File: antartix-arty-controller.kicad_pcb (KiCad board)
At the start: 2 copper layers, 50.3 x 45.6 mm, 31 parts, among them J1 QTE-020-04-L-D-A, J2 73725-0110BLF, J3 73725-0110BLF, J4 73725-0110BLF, U1 PCT2075GVX, U2 PAC1934T-I_JQ, U3 USB2514B-I_M2, U4 TPS2051BDBVR, U5 TPS2051BDBVR, U6 TPS2051BDBVR, Y1 7C-24.000MBB-T

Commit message: Add FTDI and clean up schematic
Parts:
- C1, C2, C3, C4, C5, C6, C7, C8: footprint antmicro-footprints:0402-cap -> antartix-arty-controller-footprints:0402-cap
- D1: footprint antmicro-footprints:LED_0603 -> antartix-arty-controller-footprints:LED_0603
- J1: footprint antmicro-footprints:QTE-020-04-L-D-A -> antartix-arty-controller-footprints:QTE-020-04-L-D-A
- J2, J3, J4: footprint antmicro-footprints:USB_A_Female_Vertical_RA_73725-0110BLF -> antartix-arty-controller-footprints:USB_A_Female_Vertical_RA_73725-0110BLF
- R1, R10, R11, R2, R3, R4, R5, R9: footprint antmicro-footprints:0402-res -> antartix-arty-controller-footprints:0402-res
- R6, R7, R8: footprint antmicro-footprints:1206-res -> antartix-arty-controller-footprints:1206-res
- U1: footprint antmicro-footprints:SOT95P275X110-6N -> antartix-arty-controller-footprints:SOT95P275X110-6N
- U2: footprint antmicro-footprints:QFN65P400X400X55-17N -> antartix-arty-controller-footprints:QFN65P400X400X55-17N
- U3: footprint antmicro-footprints:QFN50P600X600X100-37N -> antartix-arty-controller-footprints:QFN50P600X600X100-37N
- U4, U5, U6: footprint antmicro-footprints:SOT-753 -> antartix-arty-controller-footprints:SOT-753
- Y1: footprint antmicro-footprints:7C-24.000MBB-T -> antartix-arty-controller-footprints:7C-24.000MBB-T
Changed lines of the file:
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@@
     (add_net VCC5V0)
   )
-  (module antmicro-footprints:7C-24.000MBB-T (layer F.Cu)
+  (module antartix-arty-controller-footprints:7C-24.000MBB-T (layer F.Cu)
     (at 146.325 69.8 180)
     (attr smd)
@@
     )
   )
-  (module antmicro-footprints:SOT-753 (layer F.Cu)
+  (module antartix-arty-controller-footprints:SOT-753 (layer F.Cu)
     (at 149.85 86.35)
     (attr smd)
@@
     )
   )
-  (module antmicro-footprints:SOT-753 (layer F.Cu)
+  (module antartix-arty-controller-footprints:SOT-753 (layer F.Cu)
     (at 145.75 86.35)
     (attr smd)
@@
     )
   )
-  (module antmicro-footprints:SOT-753 (layer F.Cu)
+  (module antartix-arty-controller-footprints:SOT-753 (layer F.Cu)
     (at 141.725 86.4)
     (attr smd)
@@
     )
   )
-  (module antmicro-footprints:QFN50P600X600X100-37N (layer F.Cu)
+  (module antartix-arty-controller-footprints:QFN50P600X600X100-37N (layer F.Cu)
     (at 146.2 77.125)
     (fp_text reference U3 (at -1.537438 -4.195475) (layer F.SilkS)
@@
     )
   )
-  (module antmicro-footprints:QFN65P400X400X55-17N (layer F.Cu)
+  (module antartix-arty-controller-footprints:QFN65P400X400X55-17N (layer F.Cu)
     (at 132.55 86.55 180)
     (fp_text reference U2 (at 0.371485 -3.250455) (layer F.SilkS)
@@
     )
   )
-  (module antmicro-footprints:SOT95P275X110-6N (layer F.Cu)
+  (module antartix-arty-controller-footprints:SOT95P275X110-6N (layer F.Cu)
     (at 133.47 74.525)
     (fp_text reference U1 (at -0.508 -2.286) (layer F.SilkS)
@@
     )
   )
-  (module antmicro-footprints:0402-res (layer F.Cu)
+  (module antartix-arty-controller-footprints:0402-res (layer F.Cu)
     (at 141.45 79.35 180)
     (descr "Resistor SMD 0402 (1005 Metric), square (rectangular) end terminal, IPC_7351 nominal, (Body size source: http://www.tortai-tech.com/upload/download/2011102023233369053.pdf), generated with kicad-footprint-generator")
@@
     )
   )
-  (module antmicro-footprints:0402-res (layer F.Cu)
+  (module antartix-arty-controller-footprints:0402-res (layer F.Cu)
     (at 141.45 78.35 180)
     (descr "Resistor SMD 0402 (1005 Metric), square (rectangular) end terminal, IPC_7351 nominal, (Body size source: http://www.tortai-tech.com/upload/download/2011102023233369053.pdf), generated with kicad-footprint-generator")
@@
     )
   )
-  (module antmicro-footprints:0402-res (layer F.Cu)
+  (module antartix-arty-controller-footprints:0402-res (layer F.Cu)
     (at 145.21 72.775)
     (descr "Resistor SMD 0402 (1005 Metric), square (rectangular) end terminal, IPC_7351 nominal, (Body size source: http://www.tortai-tech.com/upload/download/2011102023233369053.pdf), generated with kicad-footprint-generator")
@@
     )
   )
-  (module antmicro-footprints:1206-res (layer F.Cu)
+  (module antartix-arty-controller-footprints:1206-res (layer F.Cu)
     (at 148.9 91.625 90)
     (descr http://media.digikey.com/pdf/Data%20Sheets/Lite-On%20PDFs/LTST-C230KFKT_5-24-06.pdf)
@@
     )
   )
-  (module antmicro-footprints:1206-res (layer F.Cu)
+  (module antartix-arty-controller-footprints:1206-res (layer F.Cu)
     (at 144.775 91.375 90)
     (descr http://media.digikey.com/pdf/Data%20Sheets/Lite-On%20PDFs/LTST-C230KFKT_5-24-06.pdf)
@@
     )
   )
-  (module antmicro-footprints:1206-res (layer F.Cu)
+  (module antartix-arty-controller-footprints:1206-res (layer F.Cu)
     (at 140.775 91.725 90)
     (descr http://media.digikey.com/pdf/Data%20Sheets/Lite-On%20PDFs/LTST-C230KFKT_5-24-06.pdf)
@@
     )
   )
-  (module antmicro-footprints:0402-res (layer F.Cu)
+  (module antartix-arty-controller-footprints:0402-res (layer F.Cu)
     (at 151.075 77.625 180)
     (descr "Resistor SMD 0402 (1005 Metric), square (rectangular) end terminal, IPC_7351 nominal, (Body size source: http://www.tortai-tech.com/upload/download/2011102023233369053.pdf), generated with kicad-footprint-generator")
@@
     )
   )
-  (module antmicro-footprints:0402-res (layer F.Cu)
+  (module antartix-arty-controller-footprints:0402-res (layer F.Cu)
     (at 151.075 76.625 180)
     (descr "Resistor SMD 0402 (1005 Metric), square (rectangular) end terminal, IPC_7351 nominal, (Body size source: http://www.tortai-tech.com/upload/download/2011102023233369053.pdf), generated with kicad-footprint-generator")
@@
     )
   )
-  (module antmicro-footprints:0402-res (layer F.Cu)
+  (module antartix-arty-controller-footprints:0402-res (layer F.Cu)
     (at 151.075 75.125)
     (descr "Resistor SMD 0402 (1005 Metric), square (rectangular) end terminal, IPC_7351 nominal, (Body size source: http://www.tortai-tech.com/upload/download/2011102023233369053.pdf), generated with kicad-footprint-generator")
@@
     )
   )
-  (module antmicro-footprints:0402-res (layer F.Cu)
+  (module antartix-arty-controller-footprints:0402-res (layer F.Cu)
     (at 151.075 74.1 180)
     (descr "Resistor SMD 0402 (1005 Metric), square (rectangular) end terminal, IPC_7351 nominal, (Body size source: http://www.tortai-tech.com/upload/download/2011102023233369053.pdf), generated with kicad-footprint-generator")
@@
     )
   )
-  (module antmicro-footprints:0402-res (layer F.Cu)
+  (module antartix-arty-controller-footprints:0402-res (layer F.Cu)
     (at 168.375 88.65 90)
     (descr "Resistor SMD 0402 (1005 Metric), square (rectangular) end terminal, IPC_7351 nominal, (Body size source: http://www.tortai-tech.com/upload/download/2011102023233369053.pdf), generated with kicad-footprint-generator")
@@
     )
   )
-  (module antmicro-footprints:USB_A_Female_Vertical_RA_73725-0110BLF (layer F.Cu)
+  (module antartix-arty-controller-footprints:USB_A_Female_Vertical_RA_73725-0110BLF (layer F.Cu)
     (at 165.525 103.35)
     (descr http://portal.fciconnect.com/Comergent//fci/drawing/73725.pdf)
@@
       (net 47 VBUS3))
   )
-  (module antmicro-footprints:USB_A_Female_Vertical_RA_73725-0110BLF (layer F.Cu)
+  (module antartix-arty-controller-footprints:USB_A_Female_Vertical_RA_73725-0110BLF (layer F.Cu)
     (at 148.412499 103.35)
     (descr http://portal.fciconnect.com/Comergent//fci/drawing/73725.pdf)
@@
       (net 44 VBUS1))
   )
-  (module antmicro-footprints:USB_A_Female_Vertical_RA_73725-0110BLF (layer F.Cu)
+  (module antartix-arty-controller-footprints:USB_A_Female_Vertical_RA_73725-0110BLF (layer F.Cu)
     (at 131.299999 103.35)
     (descr http://portal.fciconnect.com/Comergent//fci/drawing/73725.pdf)
@@
       (net 41 VBUS2))
   )
-  (module antmicro-footprints:QTE-020-04-L-D-A (layer B.Cu)
+  (module antartix-arty-controller-footprints:QTE-020-04-L-D-A (layer B.Cu)
     (at 165.55 74.275 270)
     (descr "0.8MM DOUBLE ROW HS SOCKET ASSEMBLY.")
@@
     )
   )
-  (module antmicro-footprints:LED_0603 (layer F.Cu)
+  (module antartix-arty-controller-footprints:LED_0603 (layer F.Cu)
     (at 170.625 88.15 180)
     (attr smd)
@@
     )
   )
-  (module antmicro-footprints:0402-cap (layer F.Cu)
+  (module antartix-arty-controller-footprints:0402-cap (layer F.Cu)
     (at 147.3 72.775)
     (descr "Resistor SMD 0402 (1005 Metric), square (rectangular) end terminal, IPC_7351 nominal, (Body size source: http://www.tortai-tech.com/upload/download/2011102023233369053.pdf), generated with kicad-footprint-generator")
@@
     )
   )
-  (module antmicro-footprints:0402-cap (layer F.Cu)
+  (module antartix-arty-controller-footprints:0402-cap (layer F.Cu)
     (at 135.875 86.55 90)
     (descr "Resistor SMD 0402 (1005 Metric), square (rectangular) end terminal, IPC_7351 nominal, (Body size source: http://www.tortai-tech.com/upload/download/2011102023233369053.pdf), generated with kicad-footprint-generator")
@@
     )
   )
-  (module antmicro-footprints:0402-cap (layer F.Cu)
+  (module antartix-arty-controller-footprints:0402-cap (layer F.Cu)
     (at 142.65 70.625 90)
     (descr "Resistor SMD 0402 (1005 Metric), square (rectangular) end terminal, IPC_7351 nominal, (Body size source: http://www.tortai-tech.com/upload/download/2011102023233369053.pdf), generated with kicad-footprint-generator")
@@
     )
   )
-  (module antmicro-footprints:0402-cap (layer F.Cu)
+  (module antartix-arty-controller-footprints:0402-cap (layer F.Cu)
     (at 149.4 71.6 270)
     (descr "Resistor SMD 0402 (1005 Metric), square (rectangular) end terminal, IPC_7351 nominal, (Body size source: http://www.tortai-tech.com/upload/download/2011102023233369053.pdf), generated with kicad-footprint-generator")
@@
     )
   )
-  (module antmicro-footprints:0402-cap (layer F.Cu)
+  (module antartix-arty-controller-footprints:0402-cap (layer F.Cu)
     (at 146.8 67.25 180)
     (descr "Resistor SMD 0402 (1005 Metric), square (rectangular) end terminal, IPC_7351 nominal, (Body size source: http://www.tortai-tech.com/upload/download/2011102023233369053.pdf), generated with kicad-footprint-generator")
@@
     )
   )
-  (module antmicro-footprints:0402-cap (layer F.Cu)
+  (module antartix-arty-controller-footprints:0402-cap (layer F.Cu)
     (at 143.125 72.775 180)
     (descr "Resistor SMD 0402 (1005 Metric), square (rectangular) end terminal, IPC_7351 nominal, (Body size source: http://www.tortai-tech.com/upload/download/2011102023233369053.pdf), generated with kicad-footprint-generator")
@@
     )
   )
-  (module antmicro-footprints:0402-cap (layer F.Cu)
+  (module antartix-arty-controller-footprints:0402-cap (layer F.Cu)
     (at 146.225 81.8 270)
     (descr "Resistor SMD 0402 (1005 Metric), square (rectangular) end terminal, IPC_7351 nominal, (Body size source: http://www.tortai-tech.com/upload/download/2011102023233369053.pdf), generated with kicad-footprint-generator")
@@
     )
   )
-  (module antmicro-footprints:0402-cap (layer F.Cu)
+  (module antartix-arty-controller-footprints:0402-cap (layer F.Cu)
     (at 130.65 75.025 90)
     (descr "Resistor SMD 0402 (1005 Metric), square (rectangular) end terminal, IPC_7351 nominal, (Body size source: http://www.tortai-tech.com/upload/download/2011102023233369053.pdf), generated with kicad-footprint-generator")

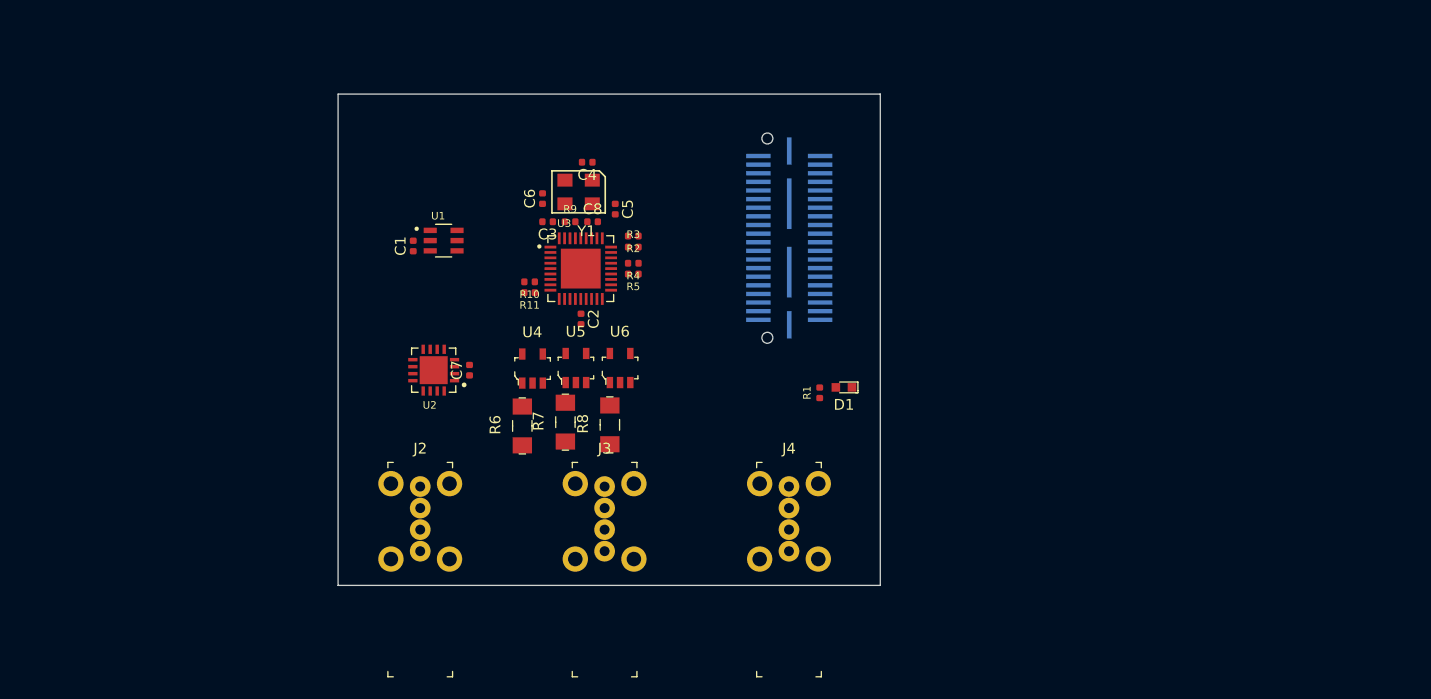
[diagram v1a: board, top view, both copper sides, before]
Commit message: Update PCB outline
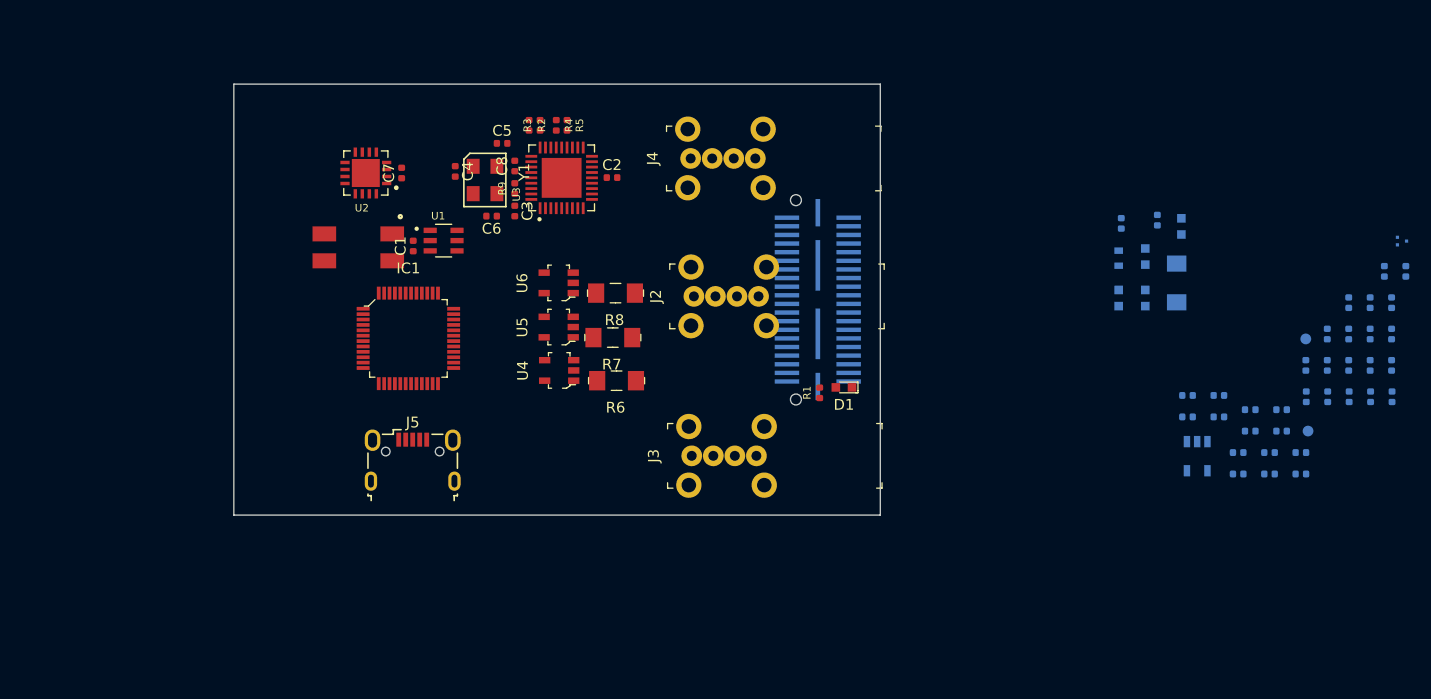
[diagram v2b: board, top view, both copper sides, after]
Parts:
- added 3V01: TP_SMD1MM, antartix-arty-controller-footprints:Testpoint_smd_1mm, B.Cu at (213.7, 92.2)
- added 5V01: TP_SMD1MM, antartix-arty-controller-footprints:Testpoint_smd_1mm, B.Cu at (213.4, 83.7)
- added C10: C_100n_0402, antartix-arty-controller-footprints:0402-cap, B.Cu at (217.5, 80.3)
- added C11: C_100n_0402, antartix-arty-controller-footprints:0402-cap, B.Cu at (217.5, 83.2)
- added C12: C_100n_0402, antartix-arty-controller-footprints:0402-cap, B.Cu at (217.5, 89.0)
- added C13: C_100n_0402, antartix-arty-controller-footprints:0402-cap, B.Cu at (207.2, 96.2)
- added C14: C_100n_0402, antartix-arty-controller-footprints:0402-cap, B.Cu at (210.1, 96.2)
- added C15: C_100n_0402, antartix-arty-controller-footprints:0402-cap, B.Cu at (207.2, 94.2)
- added C16: C_100n_0402, antartix-arty-controller-footprints:0402-cap, B.Cu at (202.5, 90.9)
- added C17: C_100n_0402, antartix-arty-controller-footprints:0402-cap, B.Cu at (202.5, 88.9)
- added C18: C_100n_0402, antartix-arty-controller-footprints:0402-cap, B.Cu at (221.5, 89.0)
- added C19: C_22p_0402, antartix-arty-controller-footprints:0402-cap, B.Cu at (215.5, 83.2)
- added C20: C_100n_0402, antartix-arty-controller-footprints:0402-cap, B.Cu at (219.5, 89.0)
- added C21: C_22p_0402, antartix-arty-controller-footprints:0402-cap, B.Cu at (210.1, 94.2)
- added C22: C_100n_0402, antartix-arty-controller-footprints:0402-cap, B.Cu at (196.4, 72.9)
- added C23: C_100n_0402, antartix-arty-controller-footprints:0402-cap, B.Cu at (221.5, 86.1)
- added C24: C_100n_0402, antartix-arty-controller-footprints:0402-cap, B.Cu at (205.4, 90.9)
- added C25: C_100n_0402, antartix-arty-controller-footprints:0402-cap, B.Cu at (213.0, 96.2)
- added C26: C_100n_0402, antartix-arty-controller-footprints:0402-cap, B.Cu at (205.4, 88.9)
- added C9: C_100n_0402, antartix-arty-controller-footprints:0402-cap, B.Cu at (220.8, 77.4)
- added D2: LG_L29K-G2J1-24-Z, antartix-arty-controller-footprints:LED_0603, B.Cu at (196.1, 79.9)
- added D3: LG_L29K-G2J1-24-Z, antartix-arty-controller-footprints:LED_0603, B.Cu at (198.6, 76.0)
- added D4: LG_L29K-G2J1-24-Z, antartix-arty-controller-footprints:LED_0603, B.Cu at (198.6, 79.9)
- added D5: LG_L29K-G2J1-24-Z, antartix-arty-controller-footprints:LED_0603, B.Cu at (201.9, 73.2)
- added D6: TPD2E009, antartix-arty-controller-footprints:SOT-3, B.Cu at (222.4, 74.6)
- added FB1: BLM18PG121SN1D, antartix-arty-controller-footprints:0603-res, B.Cu at (196.1, 76.2)
- added IC1: FT2232D, antartix-arty-controller-footprints:LQFP-48_7x7mm, F.Cu at (130.2, 83.6)
- added J5: WE_629105150521, antartix-arty-controller-footprints:USB_Micro_B_Female_629105150521, F.Cu at (130.6, 94.9)
- added R12: R_470R_0402, antartix-arty-controller-footprints:0402-res, B.Cu at (219.5, 86.1)
- added R13: R_470R_0402, antartix-arty-controller-footprints:0402-res, B.Cu at (213.5, 86.1)
- added R14: R_0R01_1206, antartix-arty-controller-footprints:1206-res, B.Cu at (201.5, 78.5)
- added R15: R_4k7_0402, antartix-arty-controller-footprints:0402-res, B.Cu at (222.8, 77.4)
- added R16: R_10k_0402, antartix-arty-controller-footprints:0402-res, B.Cu at (199.7, 72.6)
- added R17: R_470R_0402, antartix-arty-controller-footprints:0402-res, B.Cu at (208.3, 90.2)
- added R18: R_1k54_0402, antartix-arty-controller-footprints:0402-res, B.Cu at (215.5, 89.0)
- added R19: R_0R_0402, antartix-arty-controller-footprints:0402-res, B.Cu at (217.5, 86.1)
- added R20: R_0R_0402, antartix-arty-controller-footprints:0402-res, B.Cu at (213.5, 89.0)
- added R21: R_0R_0402, antartix-arty-controller-footprints:0402-res, B.Cu at (219.5, 83.2)
- added R22: R_0R_0402, antartix-arty-controller-footprints:0402-res, B.Cu at (211.2, 92.2)
- added R23: R_0R_0402, antartix-arty-controller-footprints:0402-res, B.Cu at (221.5, 80.3)
- added R24: R_0R_0402, antartix-arty-controller-footprints:0402-res, B.Cu at (215.5, 86.1)
- added R25: R_220R_0402, antartix-arty-controller-footprints:0402-res, B.Cu at (211.2, 90.2)
- added R26: R_0R_0402, antartix-arty-controller-footprints:0402-res, B.Cu at (213.0, 94.2)
- added R27: R_0R_0402, antartix-arty-controller-footprints:0402-res, B.Cu at (219.5, 80.3)
- added U7: TPS2051BDBVR, antartix-arty-controller-footprints:SOT-753, B.Cu at (203.4, 94.5)
- added Y2: MQ-6.000-12-30_30_, antartix-arty-controller-footprints:Crystal_5x7mm, F.Cu at (128.7, 76.4)
- R10, R11: value R_10k_0402 -> R_470R_0402; moved to B.Cu
- moved R10 80.2 mm to (221.5, 83.2), turned to 90 degrees
- moved R11 68.1 mm to (208.3, 92.2), turned to 0 degrees
- moved J2 39.3 mm to (162.7, 79.7), turned to 90 degrees
- moved J4 36.6 mm to (162.4, 66.9), turned to 90 degrees
- moved C7 19.4 mm to (129.6, 68.2)
- moved U2 19.4 mm to (126.2, 68.2)
- moved J3 16.6 mm to (162.5, 94.5), turned to 90 degrees
- moved R5 15.1 mm to (144.9, 63.8), turned to 270 degrees
- moved R4 14.7 mm to (143.9, 63.8), turned to 270 degrees
- moved R3 14.2 mm to (142.4, 63.8), turned to 90 degrees
- moved R2 14.1 mm to (141.4, 63.8), turned to 270 degrees
- moved C2 13.4 mm to (149.1, 68.7), turned to 0 degrees
- moved C4 12.3 mm to (134.6, 68.1), turned to 270 degrees
- moved R8 12.2 mm to (149.4, 79.4), turned to 180 degrees
- moved C5 12.1 mm to (138.9, 65.5), turned to 0 degrees
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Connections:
- R10 pad 1: Net-(R10-Pad1) -> GND
- R10 pad 2: VCC3V3 -> Net-(D2-Pad2)
- R11 pad 1: Net-(R11-Pad1) -> GND
- R11 pad 2: VCC3V3 -> Net-(D3-Pad2)
- U2 pad 9: Net-(U2-Pad9) -> VBUS4
- U3 pad 20: Net-(U3-Pad20) -> /USB4_EN
- U3 pad 21: Net-(U3-Pad21) -> /OC_N4
- U3 pad 8: Net-(R10-Pad1) -> /USB_D_N_FTDI
- U3 pad 9: Net-(R11-Pad1) -> /USB_D_P_FTDI
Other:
- board size 50.3 x 45.6 mm -> 60 x 40 mm

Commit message: Fix outline
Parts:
- D6, R18, R23, R24: moved to F.Cu
- J2, J3, J4: value 73725-0110BLF -> 614004185023; footprint antartix-arty-controller-footprints:USB_A_Female_Vertical_RA_73725-0110BLF -> antmicro-footprints:614004185023
- moved R23 59.5 mm to (163.8, 65.5), turned to 0 degrees
- moved R18 59.3 mm to (161.8, 63.8), turned to 180 degrees
- moved D6 57.6 mm to (165.7, 64.5)
- moved R24 55.1 mm to (165.6, 62.8), turned to 0 degrees
- moved J5 50.0 mm to (170.3, 64.5), turned to 90 degrees
- moved IC1 39.2 mm to (168.7, 76.1), turned to 180 degrees
- moved U2 34.0 mm to (160.2, 69.5), turned to 90 degrees
- moved J3 33.3 mm to (133.7, 77.9), turned to 180 degrees
- moved C1 31.5 mm to (160.0, 86.4), turned to 0 degrees
- moved J2 31.5 mm to (133.7, 91.9), turned to 180 degrees
- moved Y2 31.0 mm to (158.7, 84.4), turned to 180 degrees
- moved C7 31.0 mm to (160.2, 72.8), turned to 0 degrees
- moved U1 30.8 mm to (160.5, 89.2), turned to 270 degrees
- moved J4 28.9 mm to (133.7, 63.9), turned to 180 degrees
- moved C4 26.3 mm to (151.0, 88.5), turned to 0 degrees
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- renumbered 3V01 to 3V1, 5V01 to 5V1
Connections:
- J2 pad 1: VBUS2 -> VBUS1
- J2 pad 2: /USB2_D_N -> /USB1_D_N
- J2 pad 3: /USB2_D_P -> /USB1_D_P
- J3 pad 1: VBUS1 -> VBUS2
- J3 pad 2: /USB1_D_P -> /USB2_D_N
- J3 pad 3: /USB1_D_N -> /USB2_D_P
- U2 pad 15: VCC5V0 -> Net-(U2-Pad15)
- U3 pad 15: VCC3V3 -> Net-(U3-Pad15)
- U3 pad 23: VCC3V3 -> Net-(U3-Pad15)
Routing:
- net Net-(SP4-Pad1): vias 0 -> 1
- net Net-(SP3-Pad1): vias 0 -> 1
- net Net-(SP2-Pad1): vias 0 -> 1
- net Net-(SP1-Pad1): vias 0 -> 1
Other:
- board size 60 x 40 mm -> 68.5 x 40 mm
